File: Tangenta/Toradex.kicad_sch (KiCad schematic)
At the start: 15 parts, among them J17 2309410-1, Q3 BSS138, T1 NTZD3154NT1G

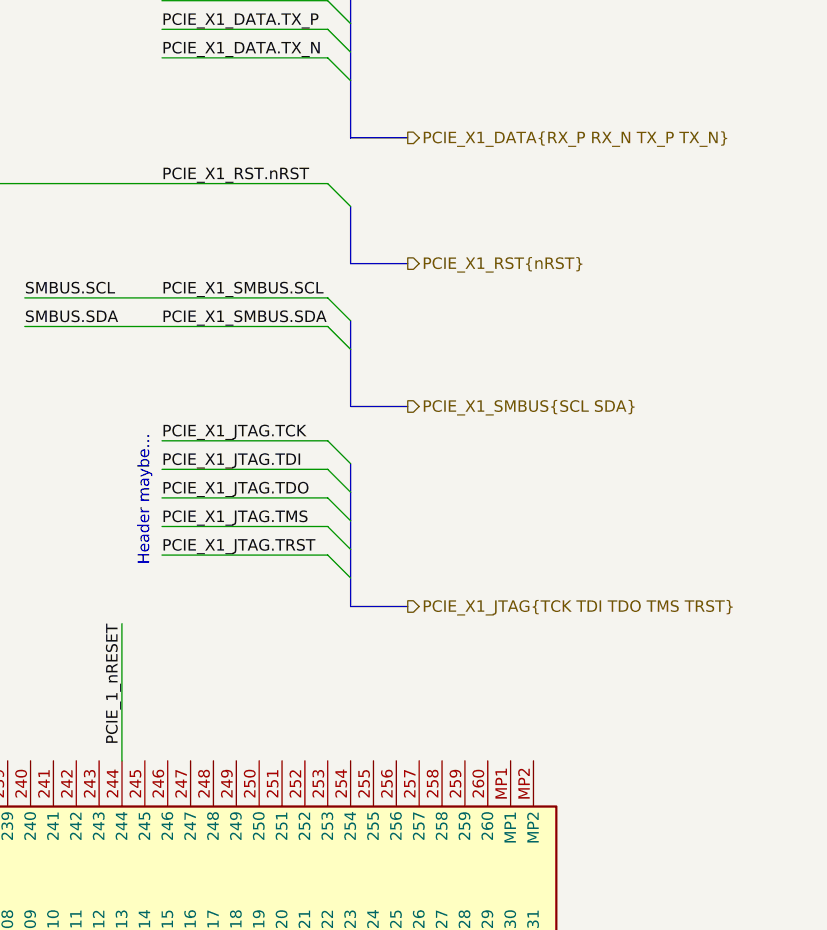
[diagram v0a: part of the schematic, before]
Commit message: PCIe nWAKE signal...
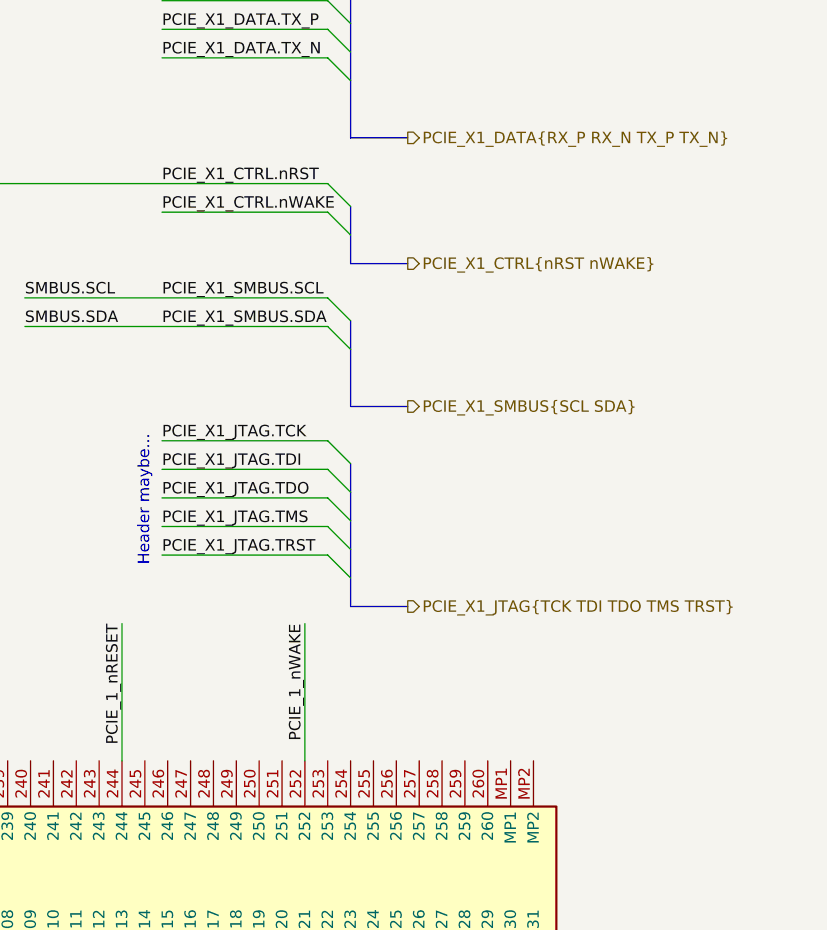
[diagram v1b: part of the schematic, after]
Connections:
- net PCIE_1_nWAKE: now reaches J17.252
- net PCIE_X1_RST.nRST renamed PCIE_X1_CTRL.nRST
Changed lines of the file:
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@@
   (junction (at 76.2 273.05) (diameter 0) (color 0 0 0 0)
   )
+  (bus_entry (at 359.41 64.77) (size -2.54 -2.54)
+    (stroke (width 0) (type default))
+  )
   (bus_entry (at 78.74 213.36) (size -2.54 -2.54)
     (stroke (width 0) (type default))
@@
     (stroke (width 0) (type default))
   )
+  (bus (pts (xy 359.41 64.77) (xy 359.41 67.945))
+    (stroke (width 0) (type default))
+  )
   (bus (pts (xy 123.19 26.67) (xy 123.19 29.21))
     (stroke (width 0) (type default))
@@
     (stroke (width 0) (type default))
   )
+  (wire (pts (xy 338.455 62.23) (xy 356.87 62.23))
+    (stroke (width 0) (type default))
+  )
   (wire (pts (xy 72.39 260.35) (xy 76.2 260.35))
     (stroke (width 0) (type default))
@@
     (stroke (width 0) (type default))
   )
+  (wire (pts (xy 354.33 123.19) (xy 354.33 107.95))
+    (stroke (width 0) (type default))
+  )
   (bus (pts (xy 123.19 20.32) (xy 123.19 22.86))
     (stroke (width 0) (type default))
@@
     (stroke (width 0) (type default))
   )
-  (bus (pts (xy 359.41 61.595) (xy 359.41 67.945))
+  (bus (pts (xy 359.41 61.595) (xy 359.41 64.77))
     (stroke (width 0) (type default))
   )
@@
     (effects (font (size 1.27 1.27)) (justify left bottom))
   )
+  (label "PCIE_1_nWAKE" (at 354.33 107.95 270) (fields_autoplaced)
+    (effects (font (size 1.27 1.27)) (justify right bottom))
+  )
   (label "USB_DR.ID" (at 20.32 25.4 0) (fields_autoplaced)
     (effects (font (size 1.27 1.27)) (justify left bottom))
@@
     (effects (font (size 1.27 1.27)) (justify left bottom))
   )
+  (label "PCIE_X1_CTRL.nWAKE" (at 338.455 62.23 0) (fields_autoplaced)
+    (effects (font (size 1.27 1.27)) (justify left bottom))
+  )
   (label "1V8" (at 54.61 236.22 0) (fields_autoplaced)
     (effects (font (size 1.27 1.27)) (justify left bottom))
@@
     (effects (font (size 1.27 1.27)) (justify right bottom))
   )
-  (label "PCIE_X1_RST.nRST" (at 338.455 59.055 0) (fields_autoplaced)
+  (label "PCIE_X1_CTRL.nRST" (at 338.455 59.055 0) (fields_autoplaced)
     (effects (font (size 1.27 1.27)) (justify left bottom))
   )
@@
     (effects (font (size 1.27 1.27)) (justify left))
   )
-  (hierarchical_label "PCIE_X1_RST{nRST}" (shape output) (at 365.76 67.945 0) (fields_autoplaced)
+  (hierarchical_label "PCIE_X1_CTRL{nRST nWAKE}" (shape output) (at 365.76 67.945 0) (fields_autoplaced)
     (effects (font (size 1.27 1.27)) (justify left))
   )

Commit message: PCIe schematic continued...
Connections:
- net PCIE_X1_SMBUS.SCL renamed SMBUS.SCL
- net PCIE_X1_SMBUS.SDA renamed SMBUS.SDA
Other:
- moved on the sheet: R2, T1A, T1B

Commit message: ...
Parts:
- added R2: 1.8k, Resistor_SMD:R_0402_1005Metric, symbol Device:R_Small_US
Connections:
- net 1V8: now also R2.2
- net PCIE_X1_CTRL.nWAKE: now also R2.1
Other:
- note added: "To a header..."
- note removed: "Header maybe..."
- moved on the sheet: R2, T1A, T1B

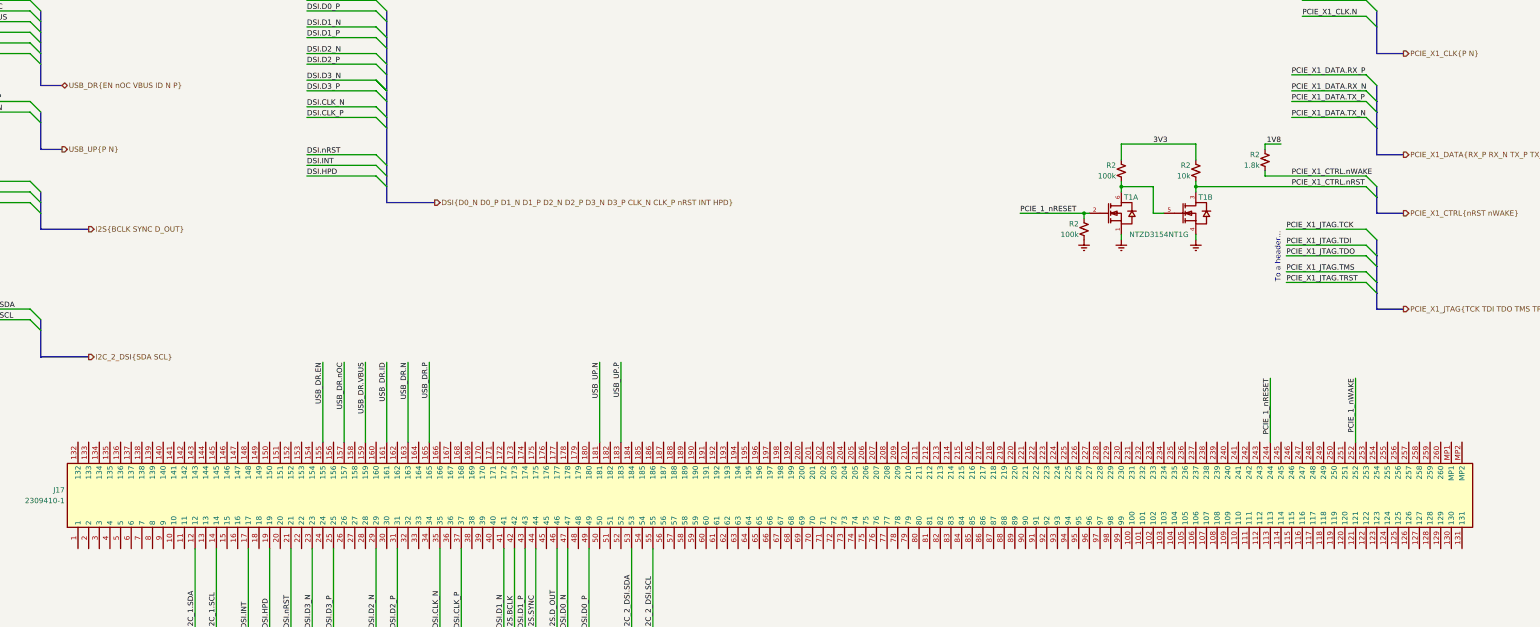
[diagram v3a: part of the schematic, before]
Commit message: PCIe at Toradex side; handling unconnected pins.
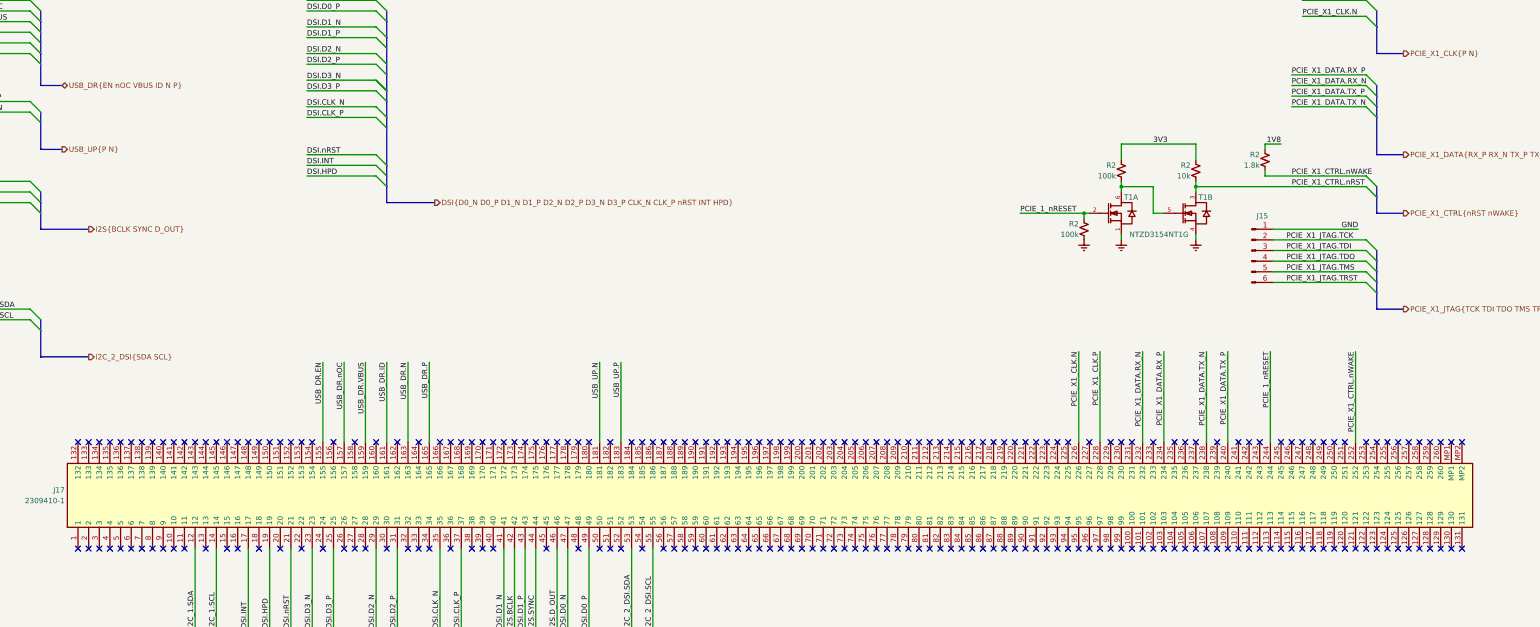
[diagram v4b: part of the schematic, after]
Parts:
- added J15: Conn_01x06_Pin, Connector_PinHeader_1.00mm:PinHeader_1x06_P1.00mm_Vertical, symbol Connector:Conn_01x06_Pin
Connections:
- net PCIE_1_nWAKE is gone; now on net PCIE_X1_CTRL.nWAKE: J17.252
- net GNDREF: now also J15.1 (Pin_1)
- net PCIE_X1_CLK.N: now also J17.226
- net PCIE_X1_CLK.P: now also J17.228
- net PCIE_X1_DATA.RX_N: now also J17.232
- net PCIE_X1_DATA.RX_P: now also J17.234
- net PCIE_X1_DATA.TX_N: now also J17.238
- net PCIE_X1_DATA.TX_P: now also J17.240
- net PCIE_X1_JTAG.TCK: now also J15.2 (Pin_2)
- net PCIE_X1_JTAG.TDI: now also J15.3 (Pin_3)
- net PCIE_X1_JTAG.TDO: now also J15.4 (Pin_4)
- net PCIE_X1_JTAG.TMS: now also J15.5 (Pin_5)
- net PCIE_X1_JTAG.TRST: now also J15.6 (Pin_6)
- no-connect marks 0 -> 226
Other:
- note removed: "To a header..."

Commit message: Schematic improvements.
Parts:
- removed J15: Conn_01x06_Pin, Connector_PinHeader_1.00mm:PinHeader_1x06_P1.00mm_Vertical, symbol Connector:Conn_01x06_Pin
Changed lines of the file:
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@@
-    (stroke (width 0) (type default))
-  )
-  (bus_entry (at 359.41 80.01) (size -2.54 -2.54)
     (stroke (width 0) (type default))
   )
@@
     (stroke (width 0) (type default))
   )
-  (bus_entry (at 359.41 82.55) (size -2.54 -2.54)
-    (stroke (width 0) (type default))
-  )
   (bus_entry (at 359.41 43.18) (size -2.54 -2.54)
     (stroke (width 0) (type default))
@@
     (stroke (width 0) (type default))
   )
-  (bus_entry (at 359.41 87.63) (size -2.54 -2.54)
-    (stroke (width 0) (type default))
-  )
   (bus_entry (at 359.41 38.1) (size -2.54 -2.54)
     (stroke (width 0) (type default))
@@
     (stroke (width 0) (type default))
   )
-  (bus_entry (at 359.41 77.47) (size -2.54 -2.54)
-    (stroke (width 0) (type default))
-  )
   (bus_entry (at 40.64 20.32) (size -2.54 -2.54)
     (stroke (width 0) (type default))
@@
     (stroke (width 0) (type default))
   )
-  (bus_entry (at 359.41 85.09) (size -2.54 -2.54)
-    (stroke (width 0) (type default))
-  )
   (bus_entry (at 359.41 24.13) (size -2.54 -2.54)
     (stroke (width 0) (type default))
@@
     (stroke (width 0) (type default))
   )
-  (wire (pts (xy 334.645 80.01) (xy 356.87 80.01))
-    (stroke (width 0) (type default))
-  )
   (wire (pts (xy 306.07 62.23) (xy 306.07 68.58))
     (stroke (width 0) (type default))
@@
     (stroke (width 0) (type default))
   )
-  (wire (pts (xy 334.645 85.09) (xy 356.87 85.09))
-    (stroke (width 0) (type default))
-  )
   (wire (pts (xy 67.31 273.05) (xy 76.2 273.05))
     (stroke (width 0) (type default))
@@
     (stroke (width 0) (type default))
   )
-  (wire (pts (xy 334.645 72.39) (xy 354.965 72.39))
-    (stroke (width 0) (type default))
-  )
   (wire (pts (xy 120.65 36.83) (xy 104.14 36.83))
     (stroke (width 0) (type default))
@@
     (stroke (width 0) (type default))
   )
-  (bus (pts (xy 359.41 87.63) (xy 359.41 91.44))
-    (stroke (width 0) (type default))
-  )
   (wire (pts (xy 120.65 24.13) (xy 104.14 24.13))
     (stroke (width 0) (type default))
@@
     (stroke (width 0) (type default))
   )
-  (bus (pts (xy 359.41 77.47) (xy 359.41 80.01))
-    (stroke (width 0) (type default))
-  )
   (wire (pts (xy 110.49 148.59) (xy 110.49 167.64))
     (stroke (width 0) (type default))
@@
     (stroke (width 0) (type default))
   )
-  (bus (pts (xy 359.41 85.09) (xy 359.41 87.63))
-    (stroke (width 0) (type default))
-  )
   (bus (pts (xy 123.19 39.37) (xy 123.19 41.91))
     (stroke (width 0) (type default))
@@
     (stroke (width 0) (type default))
   )
-  (bus (pts (xy 365.76 91.44) (xy 359.41 91.44))
-    (stroke (width 0) (type default))
-  )
   (wire (pts (xy 22.86 41.91) (xy 38.1 41.91))
     (stroke (width 0) (type default))
   )
-  (wire (pts (xy 334.645 82.55) (xy 356.87 82.55))
-    (stroke (width 0) (type default))
-  )
   (wire (pts (xy 49.53 264.16) (xy 49.53 260.35))
     (stroke (width 0) (type default))
@@
     (stroke (width 0) (type default))
   )
-  (wire (pts (xy 334.645 74.93) (xy 356.87 74.93))
-    (stroke (width 0) (type default))
-  )
   (wire (pts (xy 120.65 43.18) (xy 104.14 43.18))
     (stroke (width 0) (type default))
   )
-  (bus (pts (xy 359.41 82.55) (xy 359.41 85.09))
-    (stroke (width 0) (type default))
-  )
   (wire (pts (xy 298.45 62.23) (xy 298.45 63.5))
     (stroke (width 0) (type default))
@@
     (stroke (width 0) (type default))
   )
-  (bus (pts (xy 359.41 80.01) (xy 359.41 82.55))
-    (stroke (width 0) (type default))
-  )
-  (wire (pts (xy 334.645 77.47) (xy 356.87 77.47))
-    (stroke (width 0) (type default))
-  )
   (wire (pts (xy 76.2 273.05) (xy 92.71 273.05))
     (stroke (width 0) (type default))
@@
     (effects (font (size 1.27 1.27)) (justify left bottom))
   )
-  (label "PCIE_X1_JTAG.TDO" (at 337.82 80.01 0) (fields_autoplaced)
-    (effects (font (size 1.27 1.27)) (justify left bottom))
-  )
   (label "I2C_1.SDA" (at 77.47 167.64 90) (fields_autoplaced)
     (effects (font (size 1.27 1.27)) (justify left bottom))
@@
     (effects (font (size 1.27 1.27)) (justify left bottom))
   )
-  (label "PCIE_X1_JTAG.TMS" (at 337.82 82.55 0) (fields_autoplaced)
-    (effects (font (size 1.27 1.27)) (justify left bottom))
-  )
   (label "GND" (at 24.13 200.66 0) (fields_autoplaced)
     (effects (font (size 1.27 1.27)) (justify left bottom))
@@
     (effects (font (size 1.27 1.27)) (justify right bottom))
   )
-  (label "GND" (at 354.965 72.39 180) (fields_autoplaced)
-    (effects (font (size 1.27 1.27)) (justify right bottom))
-  )
   (label "3V3" (at 24.13 198.12 0) (fields_autoplaced)
     (effects (font (size 1.27 1.27)) (justify left bottom))
@@
     (effects (font (size 1.27 1.27)) (justify left bottom))
   )
-  (label "PCIE_X1_JTAG.TDI" (at 337.82 77.47 0) (fields_autoplaced)
-    (effects (font (size 1.27 1.27)) (justify left bottom))
-  )
   (label "SMBUS.SCL" (at 92.71 273.05 180) (fields_autoplaced)
     (effects (font (size 1.27 1.27)) (justify right bottom))
@@
     (effects (font (size 1.27 1.27)) (justify left bottom))
   )
-  (label "PCIE_X1_JTAG.TRST" (at 337.82 85.09 0) (fields_autoplaced)
-    (effects (font (size 1.27 1.27)) (justify left bottom))
-  )
   (label "PCIE_X1_CTRL.nWAKE" (at 339.09 59.69 0) (fields_autoplaced)
     (effects (font (size 1.27 1.27)) (justify left bottom))
@@
   )
   (label "DSI.D0_N" (at 166.37 167.64 90) (fields_autoplaced)
-    (effects (font (size 1.27 1.27)) (justify left bottom))
-  )
-  (label "PCIE_X1_JTAG.TCK" (at 337.82 74.93 0) (fields_autoplaced)
     (effects (font (size 1.27 1.27)) (justify left bottom))
   )
@@
   )
   (hierarchical_label "I2S{BCLK SYNC D_OUT}" (shape output) (at 52.07 72.39 0) (fields_autoplaced)
-    (effects (font (size 1.27 1.27)) (justify left))
-  )
-  (hierarchical_label "PCIE_X1_JTAG{TCK TDI TDO TMS TRST}" (shape output) (at 365.76 91.44 0) (fields_autoplaced)
     (effects (font (size 1.27 1.27)) (justify left))
   )
@@
         )
       )
-    )
-  )
-  (symbol (lib_id "Connector:Conn_01x06_Pin") (at 329.565 77.47 0) (unit 1)
-    (in_bom yes) (on_board yes) (dnp no)
-    (property "Reference" "J15" (at 332.105 69.215 0)
-      (effects (font (size 1.27 1.27)))
-    )
-    (property "Value" "Conn_01x06_Pin" (at 330.2 69.85 0)
-      (effects (font (size 1.27 1.27)) hide)
-    )
-    (property "Footprint" "Connector_PinHeader_1.00mm:PinHeader_1x06_P1.00mm_Vertical" (at 329.565 77.47 0)
-      (effects (font (size 1.27 1.27)) hide)
-    )
-    (property "Datasheet" "~" (at 329.565 77.47 0)
-      (effects (font (size 1.27 1.27)) hide)
-    )
-    (pin "1")
-    (pin "2")
-    (pin "3")
-    (pin "4")
-    (pin "5")
-    (pin "6")
-    (instances
-      (project "Tangenta"
-        (path "/358d1bcf-7599-4352-8c4d-baa18a5f09e6/db297b0b-35f2-4e86-892c-83973f1ac2db"
-          (reference "J15") (unit 1)
-        )
-      )

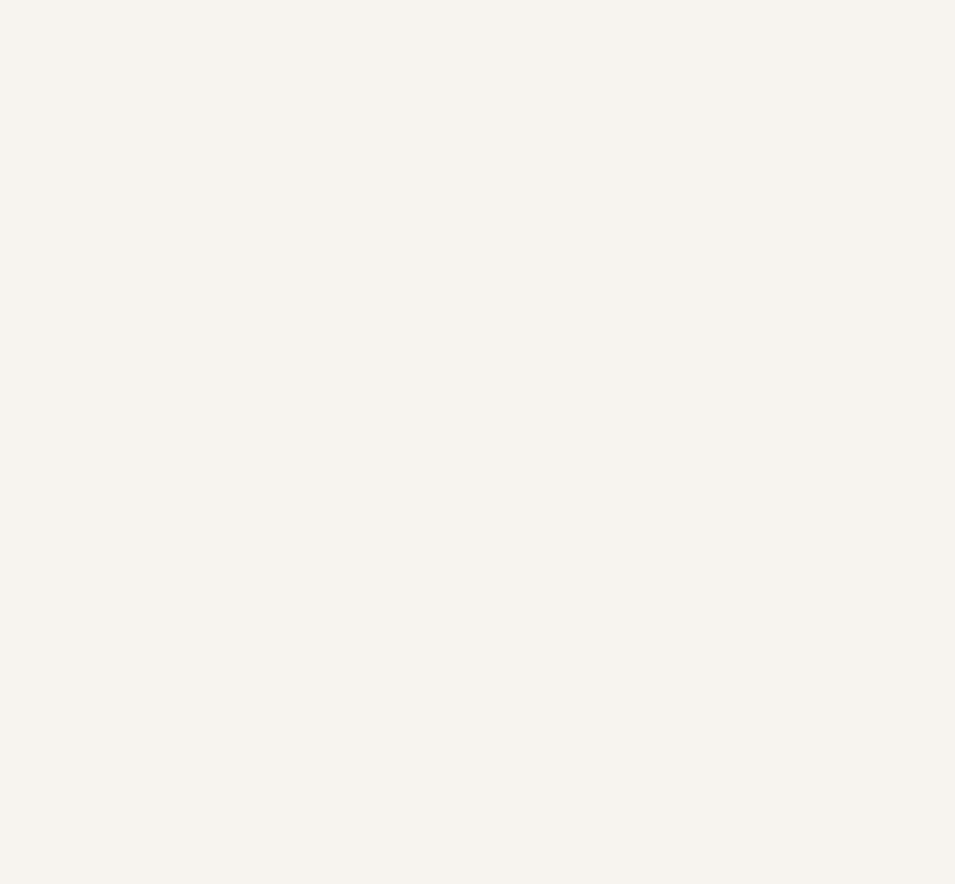
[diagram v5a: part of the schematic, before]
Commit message: Ethernet hierarchical design.
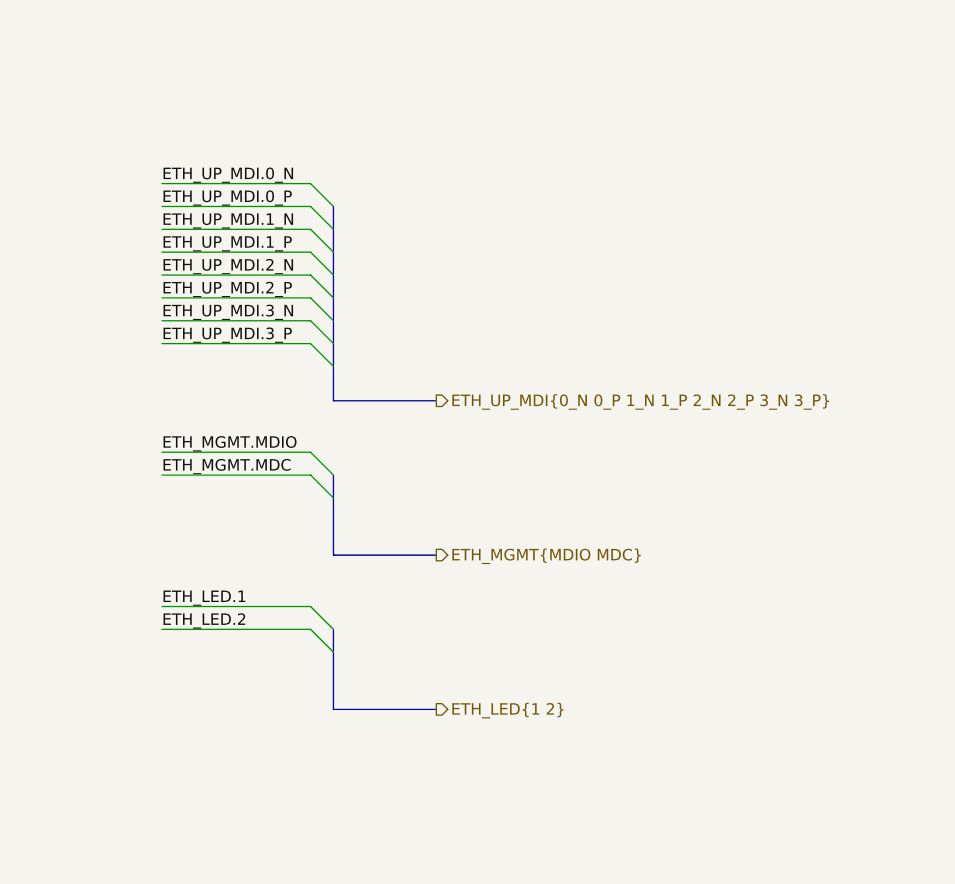
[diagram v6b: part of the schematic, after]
